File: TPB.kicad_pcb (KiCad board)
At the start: 2 copper layers, 100 x 100 mm, 11 parts, among them J200 09031967921, U200 PESD5V0S2BT, U401 XL4015

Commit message: PCB layout added
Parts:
- added C420: 330uF/25V, Capacitor_SMD:CP_Elec_8x10.5, F.Cu at (127.4, 126.2)
- added C421: 220uF/50V, Capacitor_SMD:CP_Elec_10x10.5, F.Cu at (119.1, 92.9)
- moved C417 55.9 mm to (119.9, 123.3), turned to 90 degrees
- moved R413 46.3 mm to (117.6, 120.7), turned to 90 degrees
- moved L400 44.5 mm to (110.1, 121.0), turned to 90 degrees
- moved R414 39.7 mm to (117.6, 116.0), turned to 90 degrees
- moved D403 35.0 mm to (125.8, 107.0), turned to 0 degrees
- moved C418 28.5 mm to (122.8, 103.5), turned to -90 degrees
- moved U401 25.2 mm to (111.4, 107.0), turned to 180 degrees
- moved C419 23.5 mm to (122.4, 100.4), turned to 0 degrees
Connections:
- C418 pad 1: Net-(U401-VIN) -> +12V
- C419 pad 1: Net-(U401-VIN) -> +12V
- U401 pad 5: Net-(U401-VIN) -> +12V
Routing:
- net +5V_STDBY: track 0.00 -> 44.0 mm
- net GND: track 6.73 -> 48.5 mm
- net Feedback: track 0.00 -> 17.3 mm
- net Net-(U401-SW): track 0.00 -> 13.6 mm
- net +12V: track 17.8 -> 30.9 mm
- net Net-(U401-VC): track 0.00 -> 4.15 mm
- added copper zone on F.Cu, net +12V
- added copper zone on F.Cu, net Net-(U401-SW)

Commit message: Improve to traces
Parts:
- added C400: 33nF, PCM_JLCPCB:C_0603, F.Cu at (117.8, 116.3)
- moved C420 7.04 mm to (121.4, 122.5), turned to 90 degrees
- moved R413 5.94 mm to (117.9, 114.8), turned to 180 degrees
- moved C417 5.70 mm to (118.4, 128.8), turned to 180 degrees
- moved R414 2.74 mm to (117.9, 113.3), turned to 0 degrees
- moved C418 0.27 mm to (122.8, 103.8)
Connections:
- net Feedback renamed /converter/FB
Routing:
- net GND: track 48.5 -> 403.3 mm
- net +12V: track 30.9 -> 88.8 mm
- net Net-(U401-SW): track 13.6 -> 22.8 mm
- net /converter/FB: track 17.3 -> 11.3 mm
- net +5V_STDBY: track 44.0 -> 46.8 mm
- removed copper zone on B.Cu, net (none)

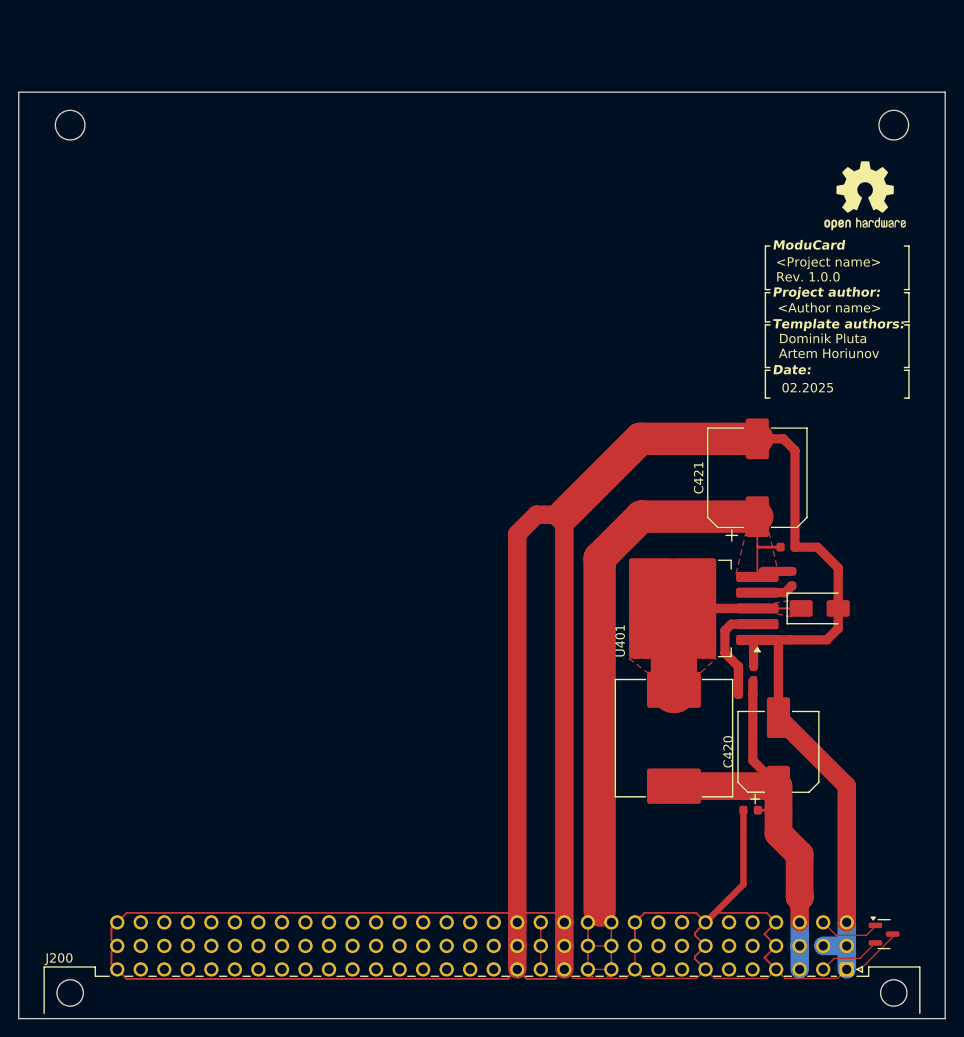
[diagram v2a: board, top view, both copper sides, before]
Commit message: Add XT60PW-F and Implement
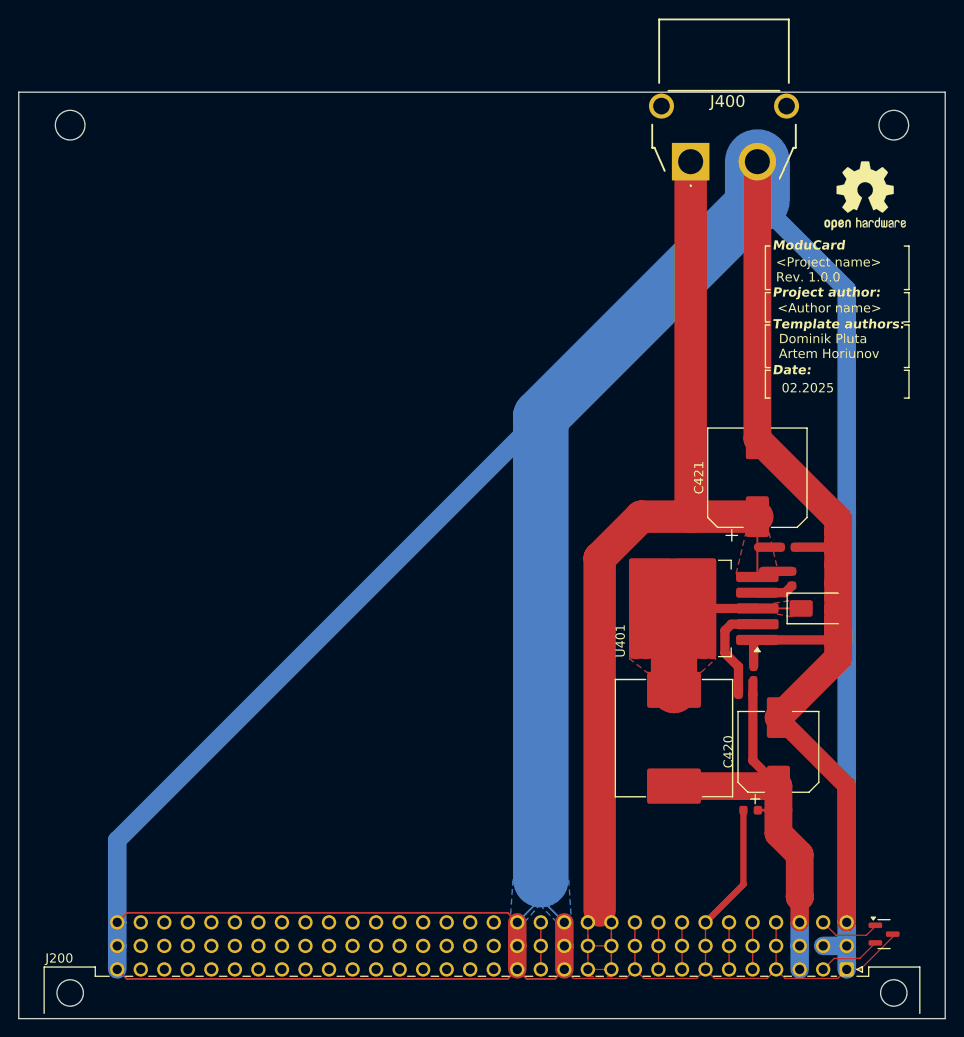
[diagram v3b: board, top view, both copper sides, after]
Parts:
- added J400: XT60PW-F, KiCad:XT60PWF, F.Cu at (111.9, 58.8)
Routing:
- net GND: track 403.3 -> 550.7 mm
- net +12V: track 88.8 -> 127.1 mm
- net /Backplane/CAN2.-: track 0.00 -> 5.08 mm
- net /Backplane/CAN2.+: track 0.00 -> 5.08 mm
- net /Backplane/CAN1.-: track 0.00 -> 5.08 mm
- net /Backplane/CAN1.+: track 0.00 -> 5.08 mm
- added copper zone on B.Cu, net GND

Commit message: change LED Indicator
also most wide tracks changed to polygons
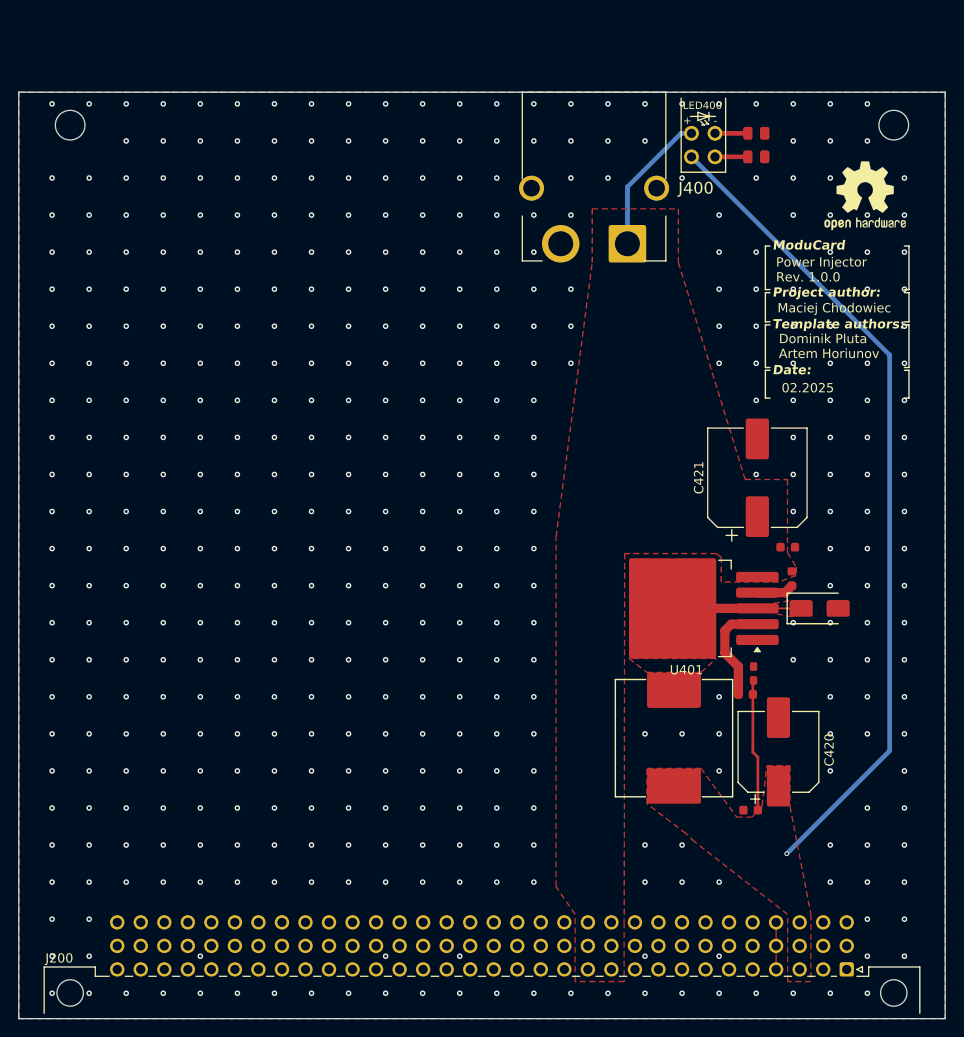
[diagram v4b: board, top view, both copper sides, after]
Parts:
- removed U200: PESD5V0S2BT, Package_TO_SOT_SMD:SOT-23
- added LED400: FixLed307, FixLed307:FixLed307, F.Cu at (113.3, 55.7)
- added R400: 1.2kΩ, PCM_JLCPCB:R_0805, F.Cu at (119.0, 58.3)
- added R401: 680Ω, PCM_JLCPCB:R_0805, F.Cu at (119.0, 55.7)
- J400: value XT60PW-F -> XT60PW-M; footprint KiCad:XT60PWF -> XT60PW-M:XT60PWM
- moved J400 13.7 mm to (101.5, 67.6)
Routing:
- net GND: track 550.7 -> 5.08 mm, vias 0 -> 452
- net +12V: track 127.1 -> 15.4 mm
- net +5V_STDBY: track 46.8 -> 102.9 mm, vias 0 -> 1
- net Net-(U401-SW): track 22.8 -> 14.1 mm
- net /Backplane/BACKPLANE.D+: track 6.82 -> 0.00 mm
- net /Backplane/BACKPLANE.D-: track 6.75 -> 0.00 mm
- net /Backplane/CAN2.-: track 5.08 -> 0.00 mm
- net /Backplane/CAN2.+: track 5.08 -> 0.00 mm
- net /Backplane/CAN1.-: track 5.08 -> 0.00 mm
- net /Backplane/CAN1.+: track 5.08 -> 0.00 mm
- net +24V: track 5.08 -> 0.00 mm
- net Net-(LED400-Pad4): track 0.00 -> 3.55 mm
- net Net-(LED400-Pad2): track 0.00 -> 3.55 mm
- added copper zone on F.Cu, net +5V_STDBY
- added copper zone on F.Cu, net GND
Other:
- board text added: "Maciej Chodowiec"
- board text added: "Power Injector Rev. ${REVISION}"
- board text removed: "<Author name>"
- board text removed: "<Project name> Rev. ${REVISION}"

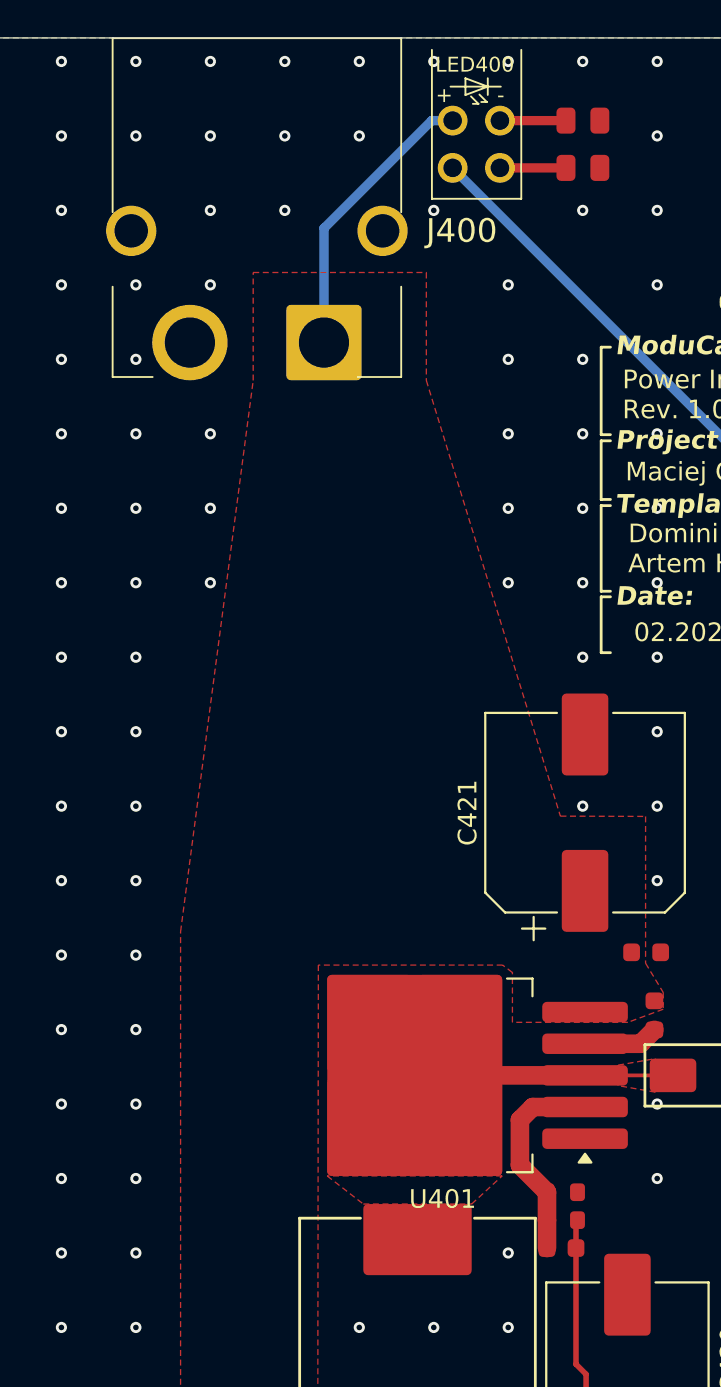
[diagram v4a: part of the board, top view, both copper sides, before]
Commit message: RDC warnings removed
All warnings and crucial errors has been removed.
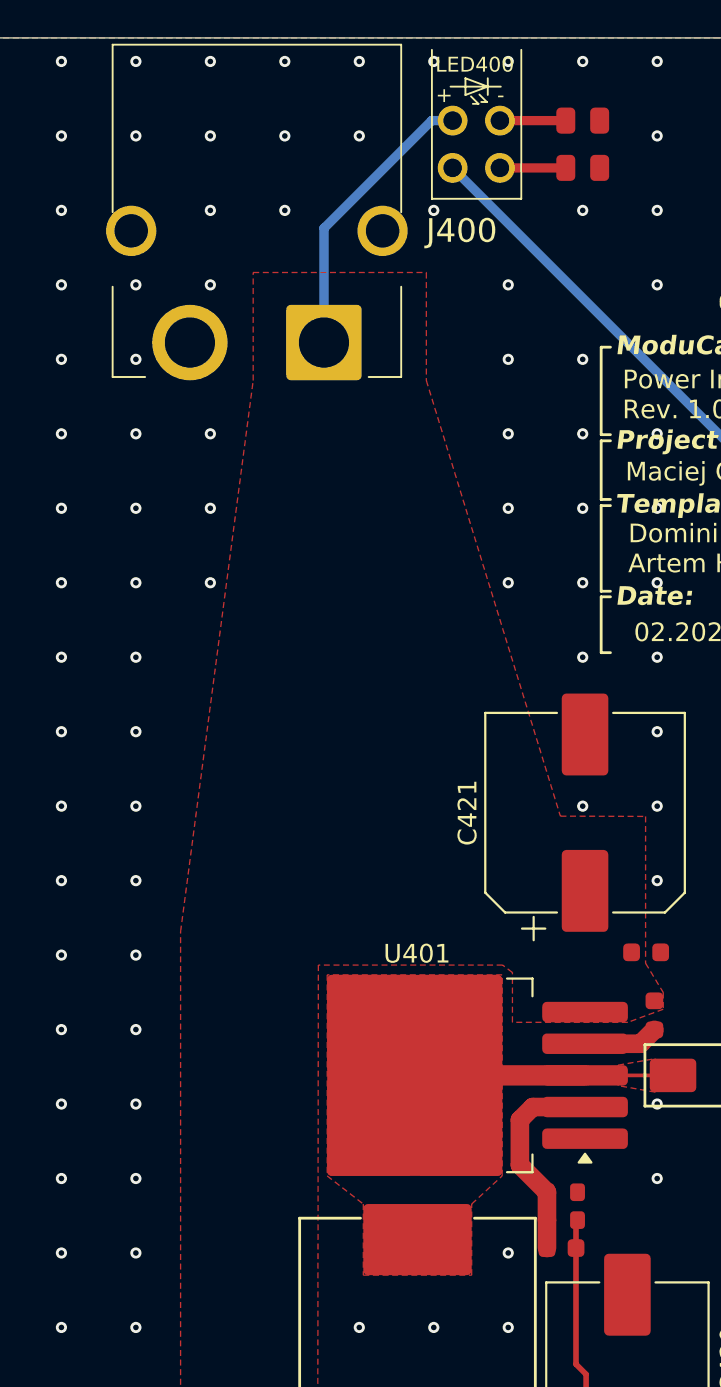
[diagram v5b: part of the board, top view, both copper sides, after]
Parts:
- moved R400 2.54 mm to (119.0, 55.7)
- moved R401 2.54 mm to (119.0, 58.3)
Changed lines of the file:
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@@
 		(tags "D2PAK DDPAK TO-263 D2PAK-5 TO-263-5 SOT-426")
 		(property "Reference" "U401"
-			(at 0 -6.65 180)
+			(at 1.375 6.525 180)
 			(layer "F.SilkS")
 			(effects
@@
 	(footprint "PCM_JLCPCB:R_0805"
 		(layer "F.Cu")
-		(at 118.98 58.265844)
+		(at 118.97 55.725844)
 		(descr "Resistor SMD 0805 (2012 Metric), square (rectangular) end terminal, IPC_7351 nominal, (Body size source: IPC-SM-782 page 72, https://www.pcb-3d.com/wordpress/wp-content/uploads/ipc-sm-782a_amendment_1_and_2.pdf), generated with kicad-footprint-generator")
 		(tags "resistor")
@@
 			)
 		)
-		(property "Height" "8.4"
-			(at 0 0 0)
-			(unlocked yes)
-			(layer "F.Fab")
-			(hide yes)
-			(effects
-				(font
-					(size 1 1)
-					(thickness 0.15)
-				)
-			)
-		)
-		(property "TME Electronic Components Part Number" ""
-			(at 0 0 0)
-			(unlocked yes)
-			(layer "F.Fab")
-			(hide yes)
-			(effects
-				(font
-					(size 1 1)
-					(thickness 0.15)
-				)
-			)
-		)
-		(property "TME Electronic Components Price/Stock" ""
-			(at 0 0 0)
-			(unlocked yes)
-			(layer "F.Fab")
-			(hide yes)
-			(effects
-				(font
-					(size 1 1)
-					(thickness 0.15)
-				)
-			)
-		)
-		(property "Manufacturer_Name" "Changzou Amass Elec"
-			(at 0 0 0)
-			(unlocked yes)
-			(layer "F.Fab")
-			(hide yes)
-			(effects
-				(font
-					(size 1 1)
-					(thickness 0.15)
-				)
-			)
-		)
-		(property "Manufacturer_Part_Number" "XT60PW-M"
-			(at 0 0 0)
-			(unlocked yes)
-			(layer "F.Fab")
-			(hide yes)
-			(effects
-				(font
-					(size 1 1)
-					(thickness 0.15)
-				)
-			)
-		)
 		(sheetname "converter")
 		(sheetfile "converter.kicad_sch")
 		(attr through_hole)
 		(fp_line
-			(start -7.75 -16.35)
-			(end 7.75 -16.35)
+			(start -7.75 -16)
+			(end 7.75 -16)
 			(stroke
 				(width 0.1)
@@
 		(fp_line
 			(start -7.75 -7)
-			(end -7.75 -16.35)
+			(end -7.75 -16)
 			(stroke
 				(width 0.1)
@@
 		(fp_line
 			(start -7.75 1.85)
-			(end -5.6 1.85)
+			(end -6 1.85)
 			(stroke
 				(width 0.1)
@@
 		)
 		(fp_line
-			(start 5.4 1.85)
+			(start 6 1.85)
 			(end 7.75 1.85)
 			(stroke
@@
 		)
 		(fp_line
-			(start 7.75 -16.35)
+			(start 7.75 -16)
 			(end 7.75 -7)
 			(stroke
@@
 		)
 		(fp_line
-			(start -7.75 -16.35)
-			(end 7.75 -16.35)
+			(start -7.75 -16)
+			(end 7.75 -16)
 			(stroke
 				(width 0.2)
@@
 		(fp_line
 			(start -7.75 1.85)
-			(end -7.75 -16.35)
+			(end -7.75 -16)
 			(stroke
 				(width 0.2)
@@
 		)
 		(fp_line
-			(start 7.75 -16.35)
+			(start 7.75 -16)
 			(end 7.75 1.85)
 			(stroke
@@
 			(layer "F.SilkS")
 		)
-		(fp_rect
+		(fp_line
 			(start -2.1664 -4.45)
+			(end -2.1664 4)
+			(stroke
+				(width 0.05)
+				(type default)
+			)
+			(layer "F.CrtYd")
+		)
+		(fp_line
+			(start -2.1664 4)
 			(end 2.1336 4)
 			(stroke
@@
 				(type default)
 			)
-			(fill none)
+			(layer "F.CrtYd")
+		)
+		(fp_line
+			(start -1.55 -4.450005)
+			(end -2.1664 -4.45)
+			(stroke
+				(width 0.05)
+				(type default)
+			)
+			(layer "F.CrtYd")
+		)
+		(fp_line
+			(start 2.1336 -4.45)
+			(end 1.55 -4.450005)
+			(stroke
+				(width 0.05)
+				(type default)
+			)
+			(layer "F.CrtYd")
+		)
+		(fp_line
+			(start 2.1336 4)
+			(end 2.1336 -4.45)
+			(stroke
+				(width 0.05)
+				(type default)
+			)
 			(layer "F.CrtYd")
 		)
 		(fp_arc
-			(start -1.516409 -4.500015)
-			(mid -0.0164 -6.000019)
-			(end 1.483609 -4.500015)
+			(start -1.55 -4.450005)
+			(mid 0 -6)
+			(end 1.55 -4.450005)
 			(stroke
 				(width 0.05)
@@
 			(layer "F.CrtYd")
 		)
-		(fp_text user "-"
-			(at 1.1 -0.9 0)
+		(fp_text user "+"
+			(at -2.2 -0.9 0)
 			(unlocked yes)
 			(layer "F.SilkS")
@@
 			)
 		)
-		(fp_text user "+"
-			(at -2.2 -0.9 0)
+		(fp_text user "-"
+			(at 1.1 -0.9 0)
 			(unlocked yes)
 			(layer "F.SilkS")
@@
 		)
 		(group ""
-			(members "47d3a815-81be-4ed8-8c57-4b84f93f2de8" "4e5b3741-ac77-4791-ae5a-41d24c19321c"
-				"83930a1d-614c-45a9-8293-96e70d12b3cc" "b9a4d078-2940-47ec-88f2-0226340635c6"
+			(members "4725651d-403e-4866-a674-c8c076d23451" "53b8f7b9-c524-4bbe-90d1-820bbf164373"
+				"ab9be0ba-4cd3-4edb-ac95-7fbb2d0afb11" "ba4b3e10-dc78-488b-9a14-0cf91436f8ba"
 			)
 		)
@@
 	(footprint "PCM_JLCPCB:R_0805"
 		(layer "F.Cu")
-		(at 118.98 55.725844)
+		(at 118.97 58.265844)
 		(descr "Resistor SMD 0805 (2012 Metric), square (rectangular) end terminal, IPC_7351 nominal, (Body size source: IPC-SM-782 page 72, https://www.pcb-3d.com/wordpress/wp-content/uploads/ipc-sm-782a_amendment_1_and_2.pdf), generated with kicad-footprint-generator")
 		(tags "resistor")
@@
 		(start 119.095 107.010001)
 		(end 109.945 107.010001)
-		(width 1)
+		(width 1.1)
 		(layer "F.Cu")
 		(net 60)
@@
 	)
 	(segment
-		(start 118.07 58.265844)
-		(end 114.5236 58.265844)
+		(start 114.5236 58.265844)
+		(end 118.06 58.265844)
 		(width 0.5)
 		(layer "F.Cu")
@@
 	)
 	(segment
-		(start 118.07 55.725844)
-		(end 114.5236 55.725844)
+		(start 114.5236 55.725844)
+		(end 118.06 55.725844)
 		(width 0.5)
 		(layer "F.Cu")
@@
 		(layer "F.Cu")
 		(hatch edge 0.5)
-		(priority 1)
+		(priority 5)
 		(connect_pads yes
 			(clearance 0.2)
@@
 		(polygon
 			(pts
-				(xy 113.005 113.920001) (xy 114.645 112.410001) (xy 105.245 112.410001) (xy 107.185 113.920001)
+				(xy 114.645 101.610001) (xy 105.245 101.610001) (xy 105.245 112.410001) (xy 107.185 113.920001)
+				(xy 107.185 117.740001) (xy 113.005 117.740001) (xy 113.005 113.920001) (xy 114.645 112.410001)
 			)
 		)
